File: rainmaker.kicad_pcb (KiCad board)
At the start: 2 copper layers, 78.7 x 25.4 mm, 3 parts, among them J1 Micro_SD_Card, U1 C3 Pico

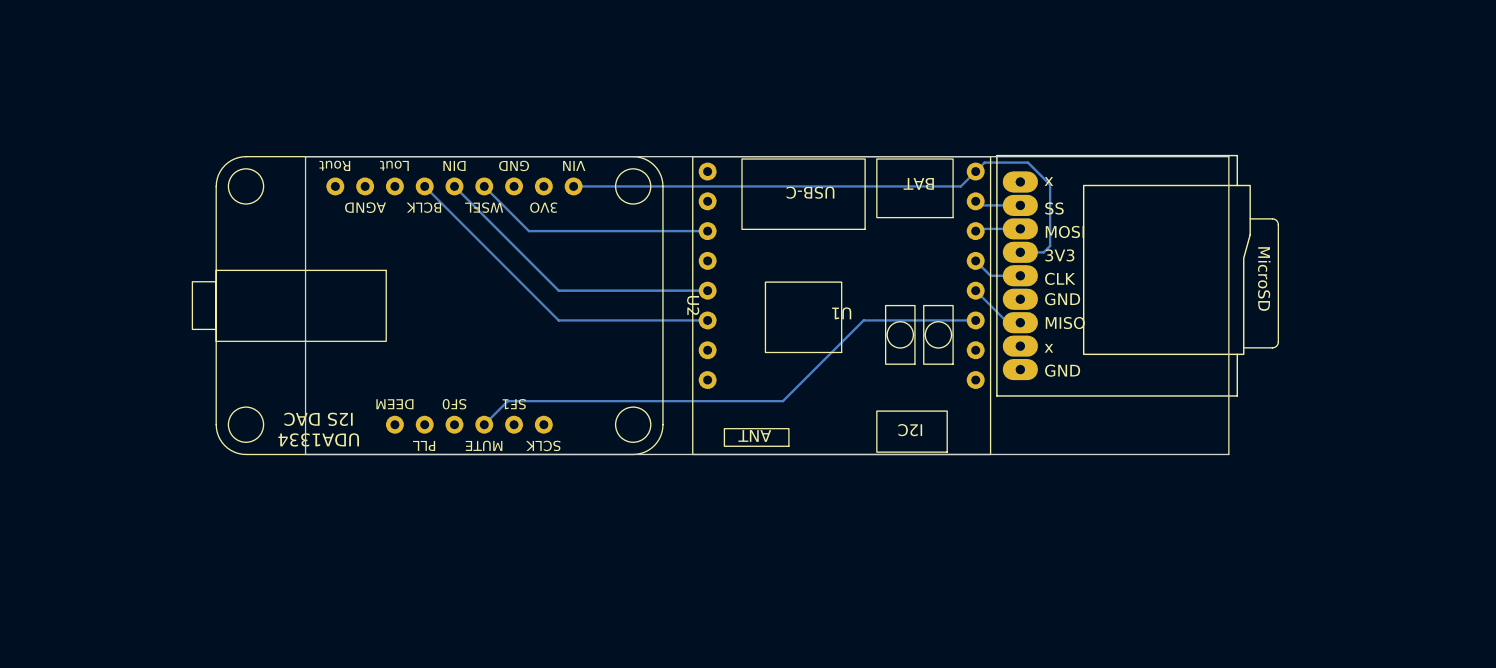
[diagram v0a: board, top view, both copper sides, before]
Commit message: Add initial pcb with routing
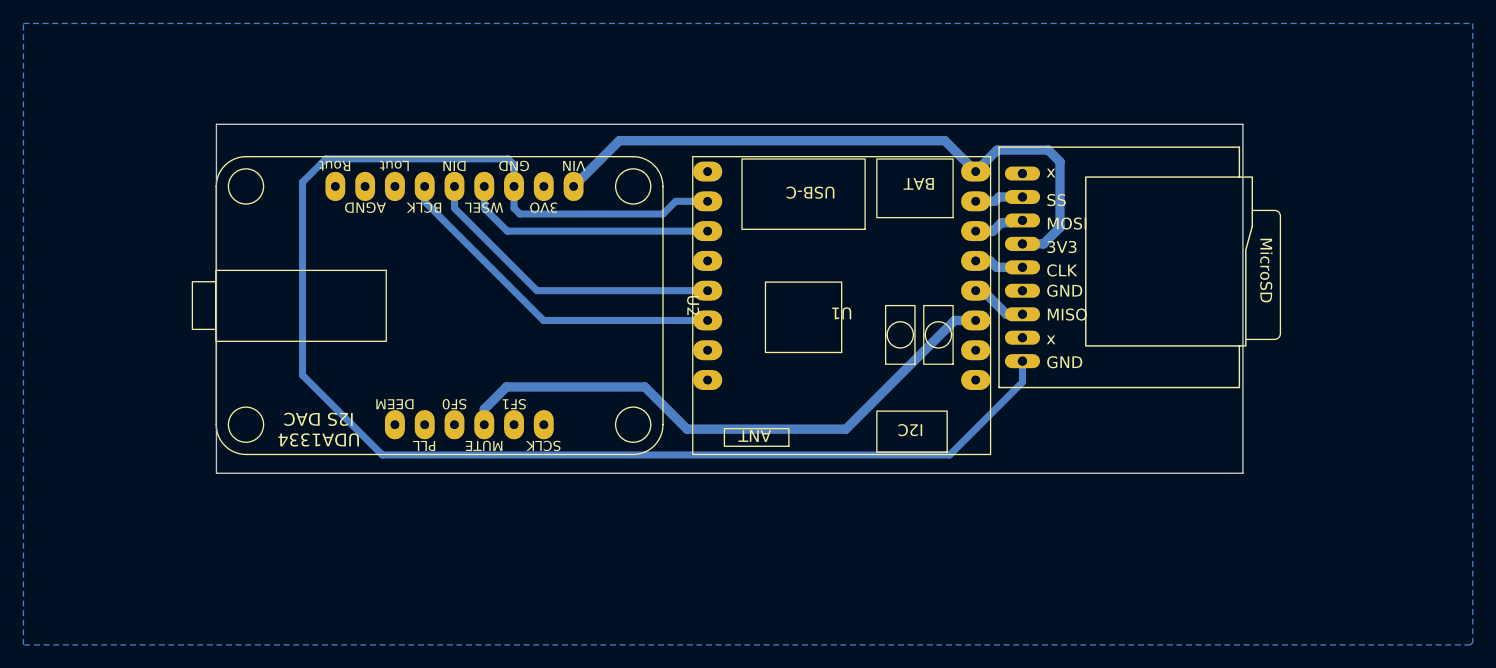
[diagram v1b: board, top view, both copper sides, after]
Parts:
- moved J1 0.74 mm to (109.4, 45.0)
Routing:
- net GND: track 0.00 -> 125.0 mm
- net +3V3: track 50.2 -> 54.7 mm
- net MUTE: track 45.6 -> 49.3 mm
- net WSEL: track 20.6 -> 21.7 mm
- net DATA: track 25.3 -> 26.4 mm
- net BCLK: track 28.9 -> 29.6 mm
- added copper zone on B.Cu, net GND
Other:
- board size 78.7 x 25.4 mm -> 87.5 x 29.8 mm

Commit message: Small pcb changes
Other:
- board size 87.5 x 29.8 mm -> 87.5 x 28.5 mm
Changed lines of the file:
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@@
 	)
 	(gr_rect
-		(start 40.66 32.8)
-		(end 128.2 62.56)
+		(start 40.66 33.894482)
+		(end 128.2 62.427669)
 		(stroke
 			(width 0.05)
@@
 	)
 	(segment
+		(start 74.44 34.78)
+		(end 83.799138 34.78)
+		(width 0.8)
+		(layer "B.Cu")
+		(net 17)
+	)
+	(segment
 		(start 107.24 35)
 		(end 111.6 35)
@@
 	)
 	(segment
-		(start 75.02 34.2)
-		(end 102.78 34.2)
+		(start 71.12 38.1)
+		(end 74.44 34.78)
 		(width 0.8)
 		(layer "B.Cu")
@@
 	)
 	(segment
-		(start 102.78 34.2)
-		(end 105.41 36.83)
+		(start 83.80838 34.789242)
+		(end 103.369242 34.789242)
 		(width 0.8)
 		(layer "B.Cu")
@@
 	)
 	(segment
+		(start 83.799138 34.78)
+		(end 83.80838 34.789242)
+		(width 0.8)
+		(layer "B.Cu")
+		(net 17)
+	)
+	(segment
 		(start 111.2 43)
 		(end 109.4 43)
@@
 	)
 	(segment
-		(start 71.12 38.1)
-		(end 75.02 34.2)
+		(start 103.369242 34.789242)
+		(end 105.41 36.83)
 		(width 0.8)
 		(layer "B.Cu")

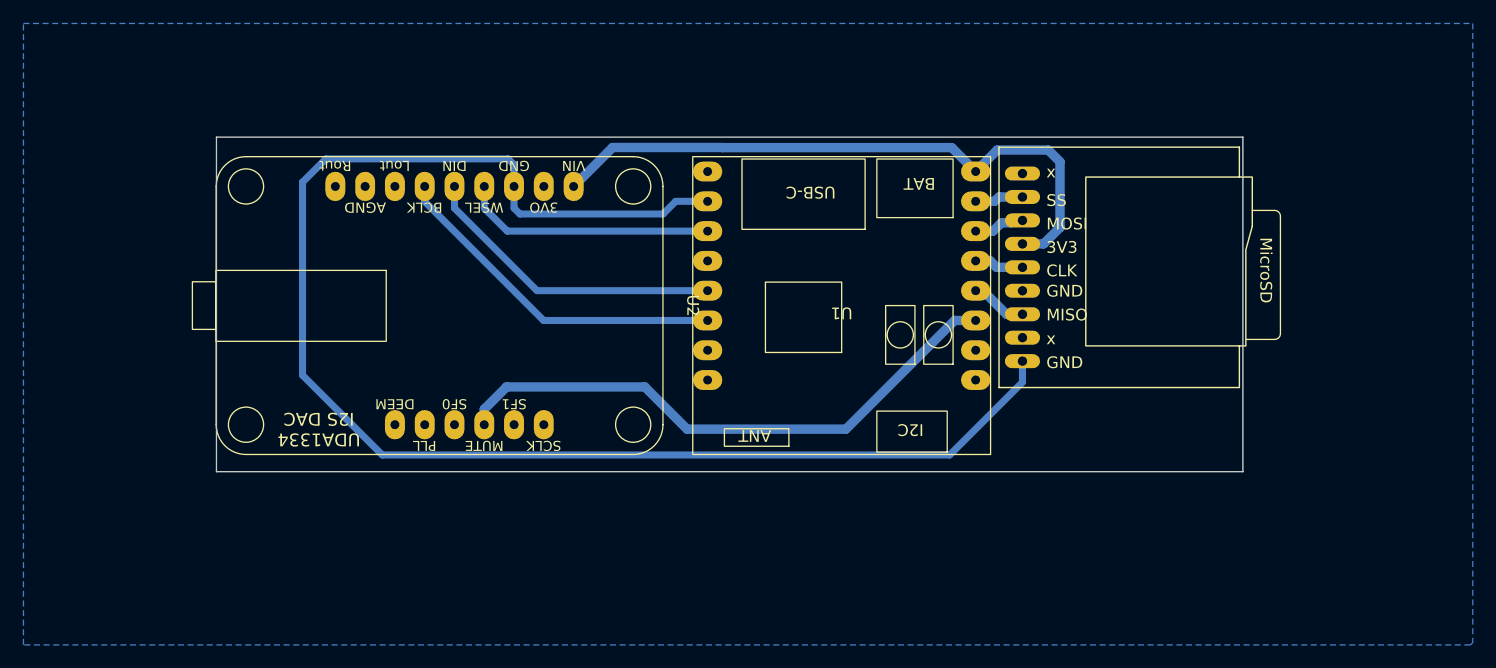
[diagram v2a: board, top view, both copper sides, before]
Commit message: Milling the PCB
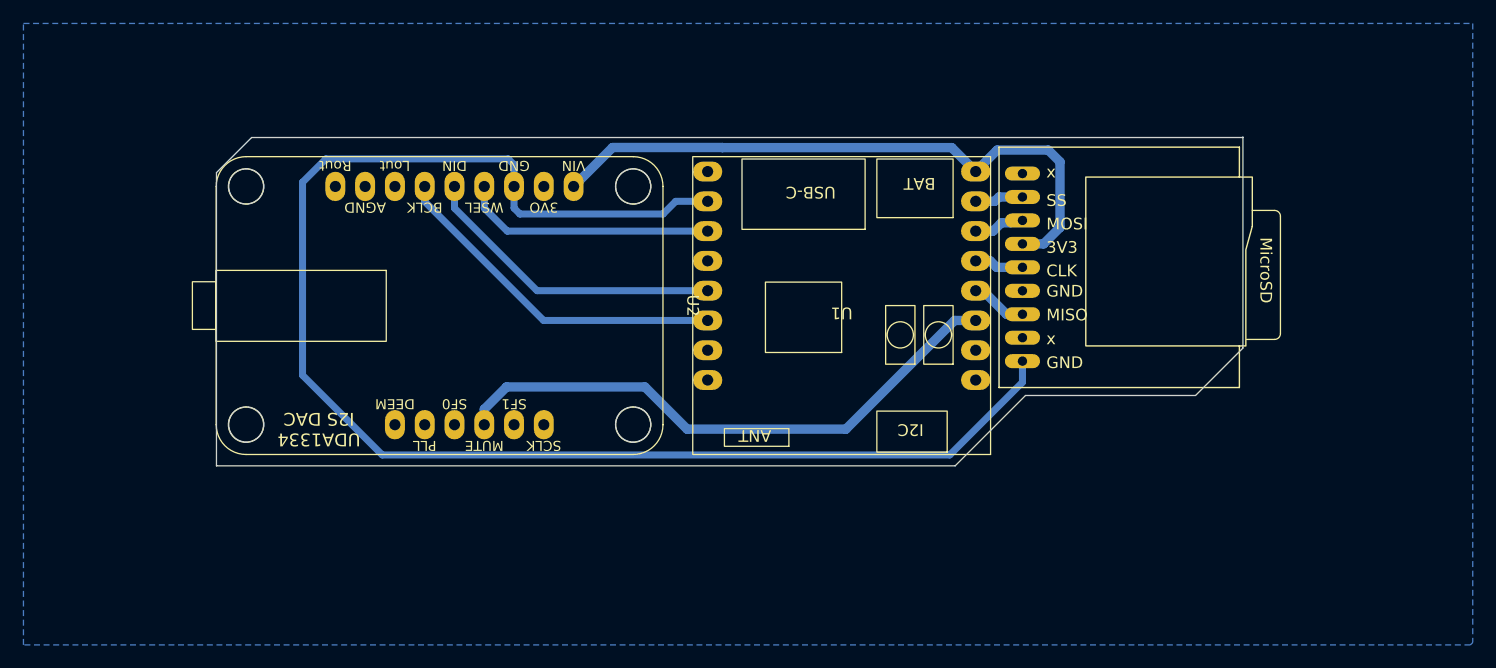
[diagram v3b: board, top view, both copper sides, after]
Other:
- board size 87.5 x 28.5 mm -> 87.5 x 28 mm
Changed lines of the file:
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@@
 		(pad_to_mask_clearance 0)
 		(allow_soldermask_bridges_in_footprints no)
+		(aux_axis_origin 40.66 61.927669)
+		(grid_origin 40.66 61.927669)
 		(pcbplotparams
-			(layerselection 0x00010fc_ffffffff)
+			(layerselection 0x0000000_fffffffe)
 			(plot_on_all_layers_selection 0x0000000_00000000)
 			(disableapertmacros no)
@@
 			(pdf_back_fp_property_popups yes)
 			(dxfpolygonmode yes)
-			(dxfimperialunits yes)
+			(dxfimperialunits no)
 			(dxfusepcbnewfont yes)
 			(psnegative no)
@@
 			(sketchpadsonfab no)
 			(subtractmaskfromsilk no)
-			(outputformat 1)
+			(outputformat 3)
 			(mirror no)
-			(drillshape 1)
+			(drillshape 0)
 			(scaleselection 1)
-			(outputdirectory "")
+			(outputdirectory "plot")
 		)
 	)
@@
 			(at 11.43 11.43 180)
 			(size 2.5 1.7)
-			(drill 0.762)
+			(drill 0.95)
 			(layers "*.Cu" "*.Mask")
 			(remove_unused_layers no)
@@
 			(at 11.43 8.89 180)
 			(size 2.5 1.7)
-			(drill 0.762)
+			(drill 0.95)
 			(layers "*.Cu" "*.Mask")
 			(remove_unused_layers no)
@@
 			(at 11.43 6.35 180)
 			(size 2.5 1.7)
-			(drill 0.762)
+			(drill 0.95)
 			(layers "*.Cu" "*.Mask")
 			(remove_unused_layers no)
@@
 			(at 11.43 3.81 180)
 			(size 2.5 1.7)
-			(drill 0.762)
+			(drill 0.95)
 			(layers "*.Cu" "*.Mask")
 			(remove_unused_layers no)
@@
 			(at 11.43 1.27 180)
 			(size 2.5 1.7)
-			(drill 0.762)
+			(drill 0.95)
 			(layers "*.Cu" "*.Mask")
 			(remove_unused_layers no)
@@
 			(at 11.43 -1.27 180)
 			(size 2.5 1.7)
-			(drill 0.762)
+			(drill 0.95)
 			(layers "*.Cu" "*.Mask")
 			(remove_unused_layers no)
@@
 			(at 11.43 -3.81 180)
 			(size 2.5 1.7)
-			(drill 0.762)
+			(drill 0.95)
 			(layers "*.Cu" "*.Mask")
 			(remove_unused_layers no)
@@
 			(at 11.43 -6.35 180)
 			(size 2.5 1.7)
-			(drill 0.762)
+			(drill 0.95)
 			(layers "*.Cu" "*.Mask")
 			(remove_unused_layers no)
@@
 			(at -11.43 11.43 180)
 			(size 2.5 1.7)
-			(drill 0.762)
+			(drill 0.95)
 			(layers "*.Cu" "*.Mask")
 			(remove_unused_layers no)
@@
 			(at -11.43 8.89 180)
 			(size 2.5 1.7)
-			(drill 0.762)
+			(drill 0.95)
 			(layers "*.Cu" "*.Mask")
 			(remove_unused_layers no)
@@
 			(at -11.43 6.35 180)
 			(size 2.5 1.7)
-			(drill 0.762)
+			(drill 0.95)
 			(layers "*.Cu" "*.Mask")
 			(remove_unused_layers no)
@@
 			(at -11.43 3.81 180)
 			(size 2.5 1.7)
-			(drill 0.762)
+			(drill 0.95)
 			(layers "*.Cu" "*.Mask")
 			(remove_unused_layers no)
@@
 			(at -11.43 1.27 180)
 			(size 2.5 1.7)
-			(drill 0.762)
+			(drill 0.95)
 			(layers "*.Cu" "*.Mask")
 			(remove_unused_layers no)
@@
 			(at -11.43 -1.27 180)
 			(size 2.5 1.7)
-			(drill 0.762)
+			(drill 0.95)
 			(layers "*.Cu" "*.Mask")
 			(remove_unused_layers no)
@@
 			(at -11.43 -3.81 180)
 			(size 2.5 1.7)
-			(drill 0.762)
+			(drill 0.95)
 			(layers "*.Cu" "*.Mask")
 			(remove_unused_layers no)
@@
 			(at -11.43 -6.35 180)
 			(size 2.5 1.7)
-			(drill 0.762)
+			(drill 0.95)
 			(layers "*.Cu" "*.Mask")
 			(remove_unused_layers no)
@@
 			(at -10.16 -10.16 270)
 			(size 2.5 1.7)
-			(drill 0.762)
+			(drill 0.95)
 			(layers "*.Cu" "*.Mask")
 			(remove_unused_layers no)
@@
 			(at -10.16 -7.62 270)
 			(size 2.5 1.7)
-			(drill 0.762)
+			(drill 0.95)
 			(layers "*.Cu" "*.Mask")
 			(remove_unused_layers no)
@@
 			(at -10.16 -5.08 270)
 			(size 2.5 1.7)
-			(drill 0.762)
+			(drill 0.95)
 			(layers "*.Cu" "*.Mask")
 			(remove_unused_layers no)
@@
 			(at -10.16 -2.54 270)
 			(size 2.5 1.7)
-			(drill 0.762)
+			(drill 0.95)
 			(layers "*.Cu" "*.Mask")
 			(remove_unused_layers no)
@@
 			(at -10.16 0 270)
 			(size 2.5 1.7)
-			(drill 0.762)
+			(drill 0.95)
 			(layers "*.Cu" "*.Mask")
 			(remove_unused_layers no)
@@
 			(at -10.16 2.54 270)
 			(size 2.5 1.7)
-			(drill 0.762)
+			(drill 0.95)
 			(layers "*.Cu" "*.Mask")
 			(remove_unused_layers no)
@@
 			(at -10.16 5.08 270)
 			(size 2.5 1.7)
-			(drill 0.762)
+			(drill 0.95)
 			(layers "*.Cu" "*.Mask")
 			(remove_unused_layers no)
@@
 			(at -10.16 7.62 270)
 			(size 2.5 1.7)
-			(drill 0.762)
+			(drill 0.95)
 			(layers "*.Cu" "*.Mask")
 			(remove_unused_layers no)
@@
 			(at -10.16 10.16 270)
 			(size 2.5 1.7)
-			(drill 0.762)
+			(drill 0.95)
 			(layers "*.Cu" "*.Mask")
 			(remove_unused_layers no)
@@
 			(at 10.16 -7.62 270)
 			(size 2.5 1.7)
-			(drill 0.762)
+			(drill 0.95)
 			(layers "*.Cu" "*.Mask")
 			(remove_unused_layers no)
@@
 			(at 10.16 -5.08 270)
 			(size 2.5 1.7)
-			(drill 0.762)
+			(drill 0.95)
 			(layers "*.Cu" "*.Mask")
 			(remove_unused_layers no)
@@
 			(at 10.16 -2.54 270)
 			(size 2.5 1.7)
-			(drill 0.762)
+			(drill 0.95)
 			(layers "*.Cu" "*.Mask")
 			(remove_unused_layers no)
@@
 			(at 10.16 0 270)
 			(size 2.5 1.7)
-			(drill 0.762)
+			(drill 0.95)
 			(layers "*.Cu" "*.Mask")
 			(remove_unused_layers no)
@@
 			(at 10.16 2.54 270)
 			(size 2.5 1.7)
-			(drill 0.762)
+			(drill 0.95)
 			(layers "*.Cu" "*.Mask")
 			(remove_unused_layers no)
@@
 			(at 10.16 5.08 270)
 			(size 2.5 1.7)
-			(drill 0.762)
+			(drill 0.95)
 			(layers "*.Cu" "*.Mask")
 			(remove_unused_layers no)
@@
 		)
 	)
-	(gr_rect
-		(start 40.66 33.894482)
-		(end 128.2 62.427669)
+	(gr_circle
+		(center 76.2 38.1)
+		(end 77.7 38.1)
 		(stroke
 			(width 0.05)
@@
 		)
 		(fill none)
+		(layer "Edge.Cuts")
+	)
+	(gr_circle
+		(center 76.2 58.4)
+		(end 77.7 58.4)
+		(stroke
+			(width 0.05)
+			(type default)
+		)
+		(fill none)
+		(layer "Edge.Cuts")
+	)
+	(gr_circle
+		(center 43.2 38.1)
+		(end 44.7 38.1)
+		(stroke
+			(width 0.05)
+			(type default)
+		)
+		(fill none)
+		(layer "Edge.Cuts")
+	)
+	(gr_circle
+		(center 43.2 58.4)
+		(end 44.7 58.4)
+		(stroke
+			(width 0.05)
+			(type default)
+		)
+		(fill none)
+		(layer "Edge.Cuts")
+	)
+	(gr_poly
+		(pts
+			(xy 40.66 61.927669) (xy 40.66 36.927669) (xy 43.66 33.927669) (xy 128.166813 33.927669) (xy 128.2 33.894482)
+			(xy 128.2 51.887669) (xy 124.16 55.927669) (xy 109.66 55.927669) (xy 103.66 61.927669)
+		)
+		(stroke
+			(width 0.05)
+			(type solid)
+		)
+		(fill none)
